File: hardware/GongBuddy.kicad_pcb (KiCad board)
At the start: 2 copper layers, 50 x 80 mm, 51 parts, among them J1 USB_B_Mini, J3 2908-05WB-MG, J4 Conn_01x15, J5 Conn_01x02, J7 Conn_Coaxial, J8 Conn_01x15, Q1 MMBT3904, U1 TPS7A19, U2 USBLC6-2SC6, U3 MCP73831T-2ACI_OT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

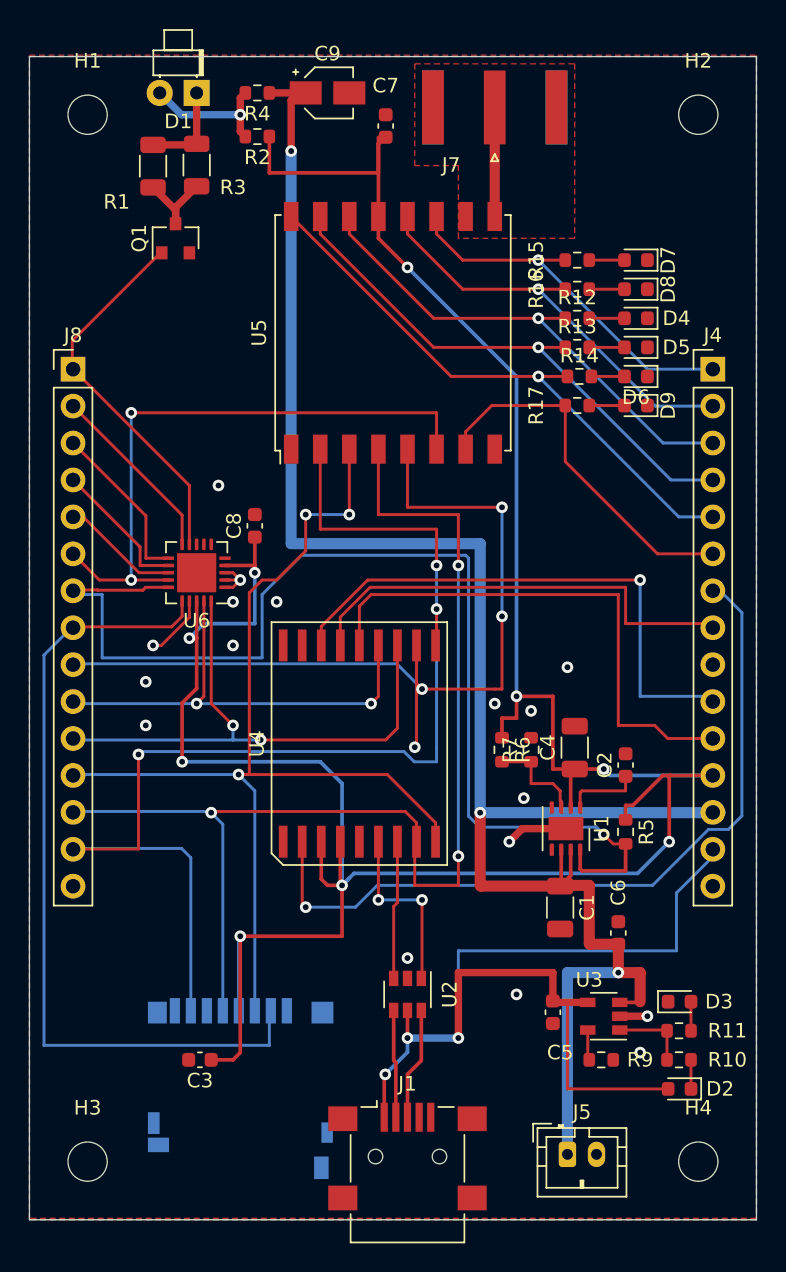
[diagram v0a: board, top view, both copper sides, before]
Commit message: Updated the mechanical design, step files, etc.
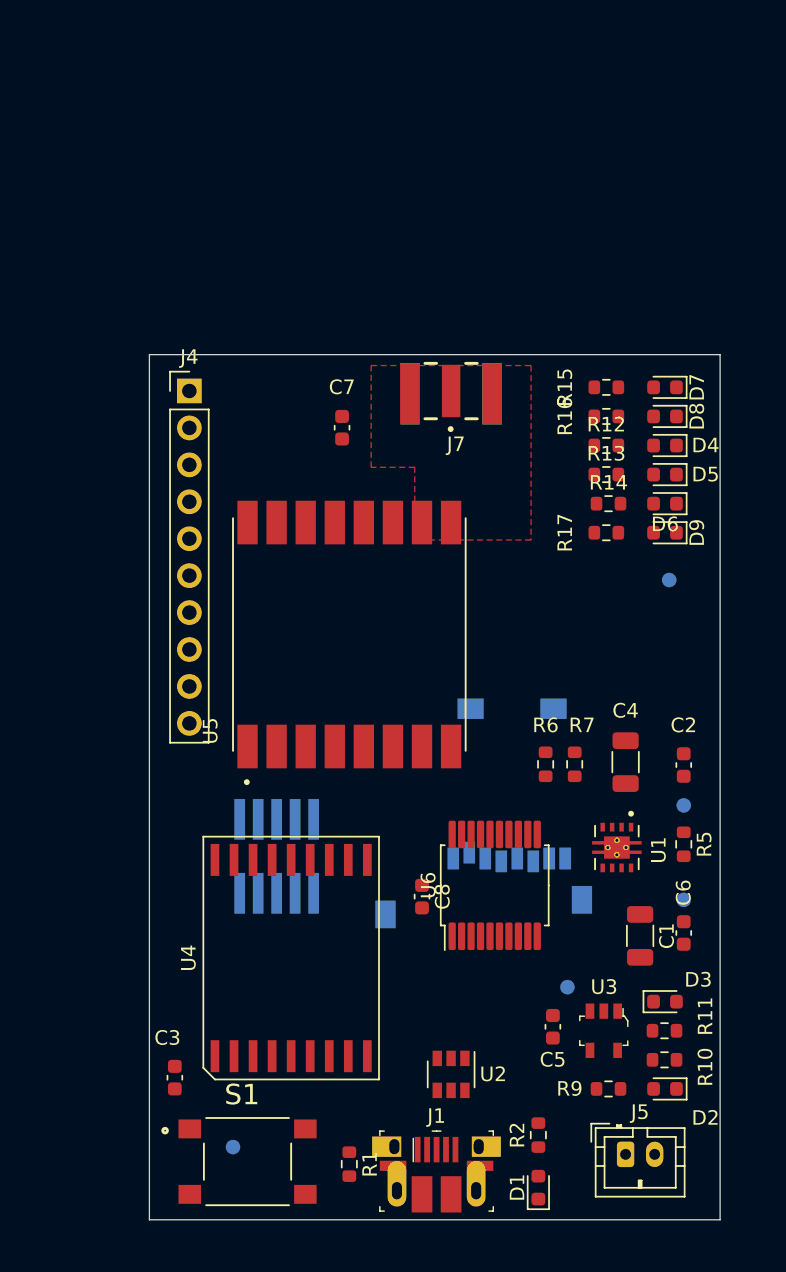
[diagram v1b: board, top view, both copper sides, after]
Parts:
- removed C9: 100u, Capacitor_SMD:CP_Elec_3x5.3
- removed H1, H2, H3, H4: MountingHole, MountingHole:MountingHole_2.7mm_M2.5
- removed J8: Conn_01x15, Connector_PinHeader_2.54mm:PinHeader_1x15_P2.54mm_Vertical
- removed Q1: MMBT3904, Package_TO_SOT_SMD:SOT-23
- removed R3: 50, Resistor_SMD:R_1206_3216Metric
- removed R4: 0, Resistor_SMD:R_0603_1608Metric
- added J2: Conn_ARM_JTAG_SWD_10, KicadFootprint:CortexSWD, B.Cu at (47.0, 115.0)
- added S1: PTS645SK50SMTR92LFS, mechanical:SW_PTS645SK50SMTR92LFS, F.Cu at (45.0, 136.0)
- added TP1: TestPoint, TestPoint:TestPoint_Pad_D1.0mm, B.Cu at (44.0, 135.0)
- added TP2: TestPoint, TestPoint:TestPoint_Pad_D1.0mm, B.Cu at (75.0, 111.5)
- added TP3: TestPoint, TestPoint:TestPoint_Pad_D1.0mm, B.Cu at (67.0, 124.0)
- added TP4: TestPoint, TestPoint:TestPoint_Pad_D1.0mm, B.Cu at (75.0, 118.0)
- added TP5: TestPoint, TestPoint:TestPoint_Pad_D1.0mm, B.Cu at (74.0, 96.0)
- D1: footprint LED_THT:LED_D1.8mm_W1.8mm_H2.4mm_Horizontal_O1.27mm_Z1.6mm -> LED_SMD:LED_0603_1608Metric
- J1: value USB_B_Mini -> 10103594-0001LF; footprint Connector_USB:USB_Mini-B_Lumberg_2486_01_Horizontal -> digikey-footprints:USB_Micro_B_Female_10103594-0001LF
- J3: footprint KicadFootprint:AMPHENOL_1140084168 -> digikey-footprints:MicroSD_2908-05WB-MG
- J4: value Conn_01x15 -> Conn_01x10; footprint Connector_PinHeader_2.54mm:PinHeader_1x15_P2.54mm_Vertical -> Connector_PinHeader_2.54mm:PinHeader_1x10_P2.54mm_Vertical
- J7: footprint Connector_Coaxial:SMA_Amphenol_132289_EdgeMount -> KicadFootprint:SAMTEC_SMA-J-P-H-ST-EM1
- R1: value 50 -> 330; footprint Resistor_SMD:R_1206_3216Metric -> Resistor_SMD:R_0603_1608Metric
- R2: value 0 -> 330
- U1: footprint Package_SON:HVSON-8-1EP_3x3mm_P0.65mm_EP1.6x2.4mm -> KicadFootprint:IC_DRV8601DRBT
- U3: footprint Package_TO_SOT_SMD:SOT-23-5 -> digikey-footprints:SOT-753
- U5: footprint RF_Module:HOPERF_RFM9XW_SMD -> KicadFootprint:XCVR_RFM95W-915S2
- U6: value MCP23008-xML -> MCP23S08; footprint Package_DFN_QFN:QFN-20-1EP_4x4mm_P0.5mm_EP2.7x2.7mm -> Package_SO:SSOP-20_5.3x7.2mm_P0.65mm
- moved D1 78.9 mm to (65.0, 137.8), turned to 90 degrees
- moved R2 71.3 mm to (65.0, 134.2), turned to 90 degrees
- moved R1 70.0 mm to (52.0, 136.2)
- moved J4 36.0 mm to (41.0, 83.0)
- moved U6 29.7 mm to (62.0, 117.0), turned to 90 degrees
- moved C8 28.0 mm to (57.0, 117.8), turned to 270 degrees
- moved C7 21.0 mm to (51.5, 85.5)
- moved U5 21.0 mm to (52.0, 99.8)
- moved J7 19.7 mm to (59.0, 83.0), turned to 180 degrees
- moved J3 18.5 mm to (59.1, 115.2)
- moved U4 15.5 mm to (48.0, 122.0)
- moved D4 8.98 mm to (73.7, 86.8)
- moved D5 8.98 mm to (73.7, 88.8)
- moved D6 8.98 mm to (73.7, 90.8)
- moved D7 8.98 mm to (73.7, 82.8)
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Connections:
- D1 pad 1: Net-(D1-Pad1) -> GND
- J4 pad 1: /DIO3 -> /DIO0
- J4 pad 10: /SWD_IO -> GND
- J4 pad 2: /DIO4 -> /DIO1
- J4 pad 3: /DIO0 -> /IO_INT
- J4 pad 4: /DIO1 -> /IO_CS
- J4 pad 5: /DIO2 -> /LORA_CS
- J4 pad 6: /DIO5 -> /SD_CS
- J4 pad 7: /VDD_OUT -> /SPI_MOSI
- J4 pad 8: /SWD_CLK -> /SPI_CLK
- J4 pad 9: GND -> /SPI_MISO
- R1 pad 1: Net-(D1-Pad1) -> VCC
- R1 pad 2: Net-(Q1-Pad3) -> /BUTTON1
- R2 pad 1: VCC -> /LED1
- U4 pad 10: /SPI_MISO -> /SPI_MOSI
- U4 pad 11: /LORA_CS -> /IO_CS
- U4 pad 12: /I2C_SDA -> /IO_RESET
- U4 pad 13: /I2C_SCL -> /IO_INT
- U4 pad 9: /SPI_MOSI -> /SPI_MISO
- U6 pad 1: GND -> /SPI_CLK
- U6 pad 10: Net-(J8-Pad2) -> (no net)
- U6 pad 11: Net-(J8-Pad3) -> (no net)
- U6 pad 12: Net-(J8-Pad4) -> /DIO0
- U6 pad 13: Net-(J8-Pad5) -> /DIO1
- U6 pad 14: /LORA_RESET -> /LED1
- U6 pad 15: /PG -> /BUTTON1
- U6 pad 16: /SD_CS -> /LORA_CS
- U6 pad 17: GND -> /LORA_RESET
- U6 pad 18: VCC -> /PG
- U6 pad 19: /I2C_SCL -> /SD_CS
- U6 pad 2: GND -> /SPI_MOSI
- U6 pad 20: /I2C_SDA -> VCC
- U6 pad 3: GND -> /SPI_MISO
- U6 pad 4: VCC -> GND
- U6 pad 5: Net-(U6-Pad5) -> GND
- U6 pad 6: Net-(U6-Pad6) -> /IO_RESET
- U6 pad 7: Net-(U6-Pad7) -> /IO_CS
- U6 pad 8: Net-(U6-Pad8) -> /IO_INT
- U6 pad 9: /BIG_LED -> GND
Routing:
- net VCC: track 194.9 -> 0.00 mm, vias 9 -> 0
- net /VBAT: track 129.7 -> 0.00 mm, vias 3 -> 0
- net /SPI_MISO: track 83.0 -> 0.00 mm, vias 3 -> 0
- net /SPI_CLK: track 80.9 -> 0.00 mm, vias 3 -> 0
- net /PG: track 79.7 -> 0.00 mm, vias 1 -> 0
- net /SPI_MOSI: track 71.9 -> 0.00 mm, vias 3 -> 0
- net VBUS: track 69.0 -> 0.00 mm, vias 3 -> 0
- net /LORA_CS: track 63.5 -> 0.00 mm, vias 4 -> 0
- net /SD_CS: track 56.4 -> 0.00 mm
- net /VDD_OUT: track 53.3 -> 0.00 mm, vias 1 -> 0
- net /LORA_RESET: track 42.4 -> 0.00 mm, vias 2 -> 0
- net /DIO2: track 40.1 -> 0.00 mm, vias 1 -> 0
- net /I2C_SDA: track 38.7 -> 0.00 mm, vias 2 -> 0
- net /SWD_IO: track 38.2 -> 0.00 mm, vias 1 -> 0
- net /DIO1: track 37.6 -> 0.00 mm, vias 1 -> 0
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- removed copper zone on B.Cu, net GND
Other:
- board size 50 x 80 mm -> 39.2 x 59.5 mm

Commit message: Added more files.
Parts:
- added TP10: TestPoint, TestPoint:TestPoint_Pad_D1.0mm, B.Cu at (66.0, 84.0)
- added TP11: TestPoint, TestPoint:TestPoint_Pad_D1.0mm, B.Cu at (67.0, 134.5)
- added TP12: TestPoint, TestPoint:TestPoint_Pad_D1.0mm, B.Cu at (66.0, 91.8)
- added TP6: TestPoint, TestPoint:TestPoint_Pad_D1.0mm, B.Cu at (42.5, 125.5)
- added TP7: TestPoint, TestPoint:TestPoint_Pad_D1.0mm, B.Cu at (52.0, 132.5)
- added TP8: TestPoint, TestPoint:TestPoint_Pad_D1.0mm, B.Cu at (66.0, 89.7)
- added TP9: TestPoint, TestPoint:TestPoint_Pad_D1.0mm, B.Cu at (66.0, 81.8)
- moved C3 23.6 mm to (56.6, 113.4)
- moved TP1 9.45 mm to (45.0, 125.6)
- moved TP4 2.06 mm to (73.0, 117.5)
- moved TP5 1.84 mm to (73.3, 94.3)
- moved R14 1.66 mm to (68.5, 89.8)
- moved C2 1.58 mm to (73.5, 108.2)
- moved C6 1.58 mm to (73.5, 120.8), turned to 270 degrees
- moved D4 1.57 mm to (72.5, 85.8)
- moved D5 1.57 mm to (72.5, 87.8)
- moved D6 1.57 mm to (72.5, 89.8)
- moved D7 1.57 mm to (72.5, 81.8)
- moved D8 1.57 mm to (72.5, 83.8)
- moved D9 1.57 mm to (72.5, 91.8)
- moved C7 1.56 mm to (52.4, 86.8)
- moved R12 1.54 mm to (68.5, 85.8)
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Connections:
- J4 pad 7: /SPI_MOSI -> /SPI_CLK
- J4 pad 8: /SPI_CLK -> /SPI_MOSI
- U1 pad 10: (no net) -> GND
- U1 pad 11: (no net) -> GND
- U1 pad 12: (no net) -> GND
- U1 pad 13: (no net) -> GND
- U6 pad 12: /DIO0 -> /PG
- U6 pad 13: /DIO1 -> /DIO0
- U6 pad 14: /LED1 -> /DIO1
- U6 pad 15: /BUTTON1 -> /LED1
- U6 pad 16: /LORA_CS -> /BUTTON1
- U6 pad 17: /LORA_RESET -> /SD_CS
- U6 pad 18: /PG -> /LORA_RESET
- U6 pad 19: /SD_CS -> /LORA_CS
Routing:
- net /DIO0: track 0.00 -> 71.8 mm, vias 0 -> 3
- net /DIO1: track 0.00 -> 68.0 mm, vias 0 -> 4
- net GND: track 0.00 -> 67.1 mm, vias 0 -> 61
- net /SPI_CLK: track 0.00 -> 63.1 mm, vias 0 -> 4
- net /IO_INT: track 0.00 -> 61.3 mm, vias 0 -> 3
- net /IO_CS: track 0.00 -> 58.5 mm, vias 0 -> 4
- net /SPI_MISO: track 0.00 -> 58.5 mm, vias 0 -> 4
- net /BUTTON1: track 0.00 -> 49.2 mm, vias 0 -> 3
- net /SD_CS: track 0.00 -> 40.5 mm, vias 0 -> 2
- net /SPI_MOSI: track 0.00 -> 37.2 mm, vias 0 -> 1
- net VBUS: track 0.00 -> 36.2 mm, vias 0 -> 4
- net /LORA_CS: track 0.00 -> 35.3 mm
- net /DIO2: track 0.00 -> 34.8 mm, vias 0 -> 2
- net /VBAT: track 0.00 -> 34.3 mm, vias 0 -> 2
- net /DIO4: track 0.00 -> 30.0 mm, vias 0 -> 2
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- added copper zone on In2.Cu, net GND
- added copper zone on In1.Cu, net VCC
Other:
- board size 39.2 x 59.5 mm -> 39 x 59 mm
- copper layers 2 -> 4
- net class Default: clearance 0.2 -> 0.127; trace_width 0.25 -> 0.1524; via_dia 0.8 -> 0.381; via_drill 0.4 -> 0.2032
- rule trace_clearance: 0.2 -> 0.127
- rule trace_min: 0.2 -> 0.1016
- rule via_min_drill: 0.3 -> 0.2032
- rule via_min_size: 0.4 -> 0.381
- board text added: "GongBuddy Rev B Copyright 2021 Nick Butts"
- board text removed: "GongBuddy Rev A Copyright 2020 Nick Butts"

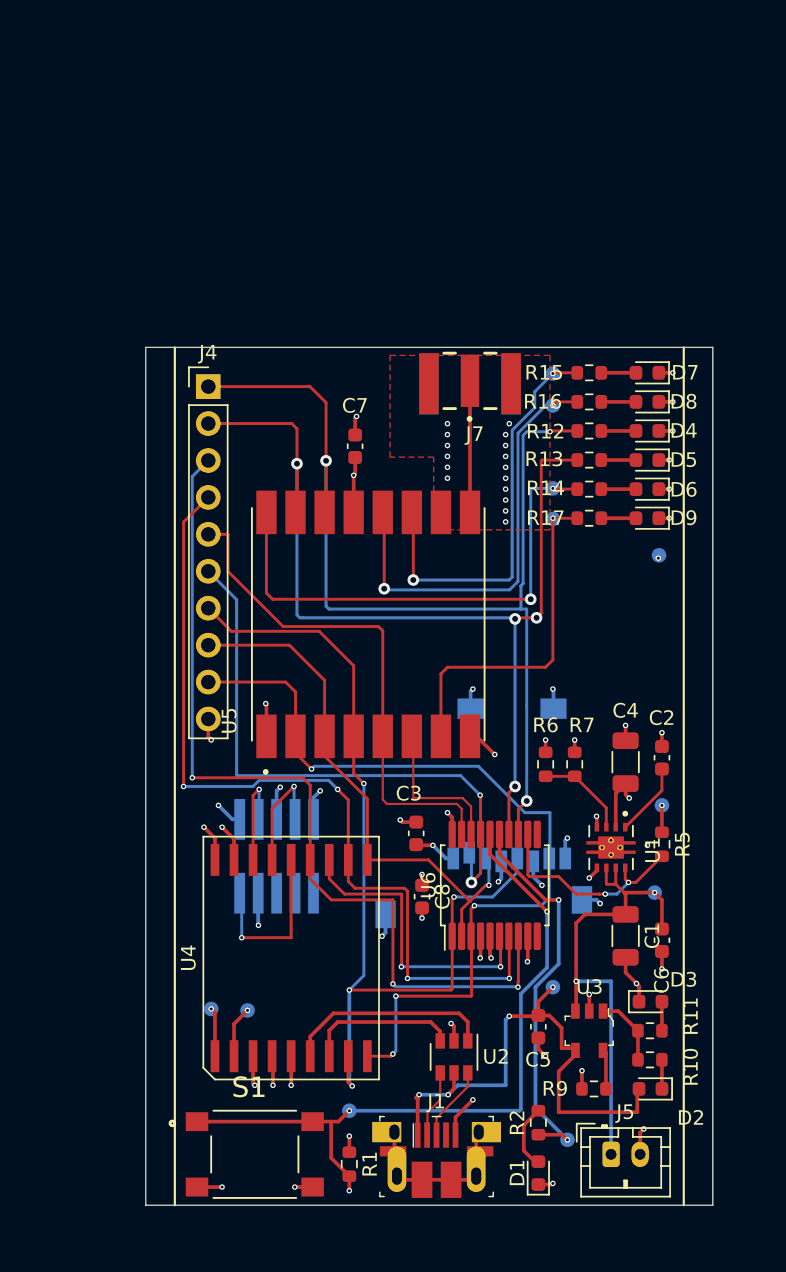
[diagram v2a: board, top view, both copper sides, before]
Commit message: Tweaked layout based on integration with the enclosure.
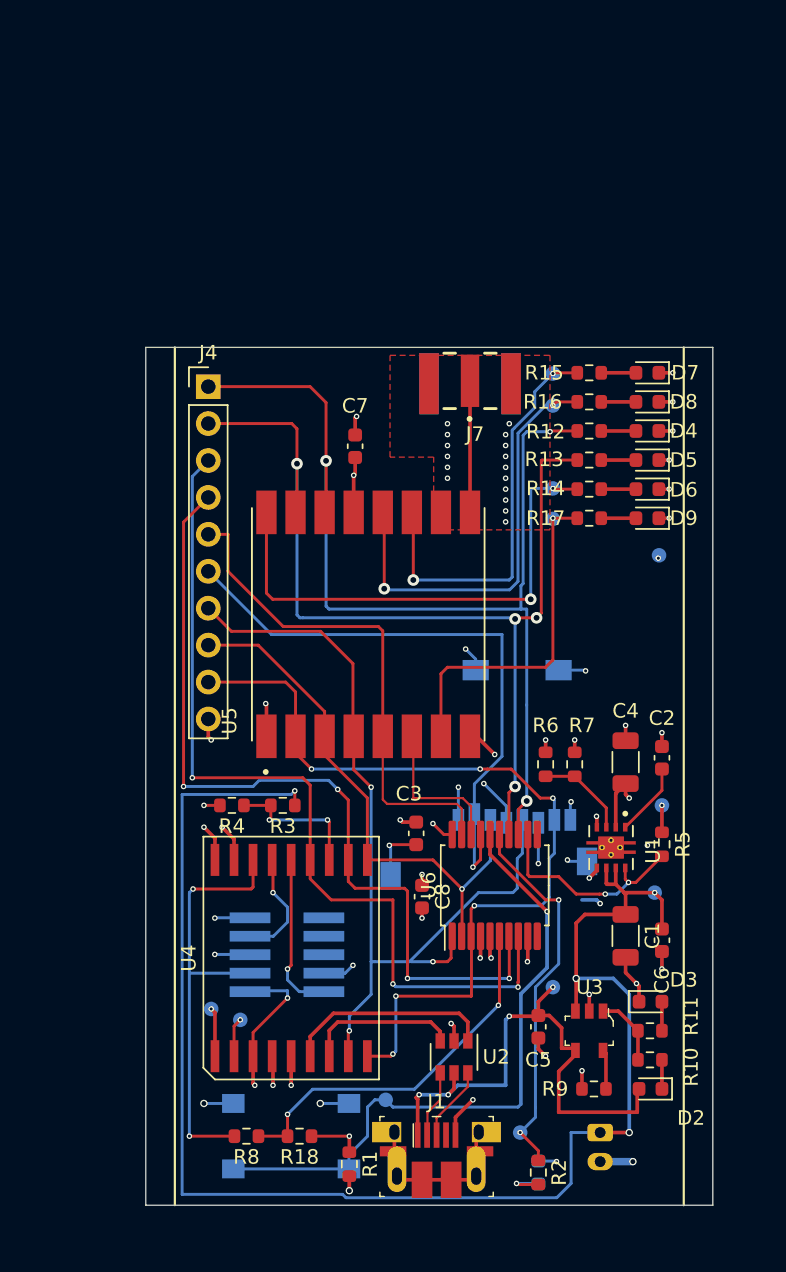
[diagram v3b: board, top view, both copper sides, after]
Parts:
- added R18: 10k, Resistor_SMD:R_0603_1608Metric, F.Cu at (48.6, 134.2)
- added R3: 49.9, Resistor_SMD:R_0603_1608Metric, F.Cu at (47.4, 111.5)
- added R4: 24.3, Resistor_SMD:R_0603_1608Metric, F.Cu at (43.9, 111.5)
- added R8: DNP, Resistor_SMD:R_0603_1608Metric, F.Cu at (44.9, 134.2)
- D1, J5, S1: moved to B.Cu
- moved J2 6.81 mm to (47.7, 121.8), turned to 90 degrees
- moved R2 3.43 mm to (65.0, 136.8), turned to 270 degrees
- moved TP11 3.29 mm to (63.8, 134.0)
- moved S1 2.80 mm to (48.0, 134.2)
- moved J3 2.67 mm to (59.5, 112.5)
- moved TP7 2.61 mm to (54.5, 131.8)
- moved J5 1.68 mm to (69.2, 134.0), turned to 270 degrees
- moved TP1 0.82 mm to (44.5, 126.2)
- turned D1 to 270 degrees
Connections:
- U4 pad 12: /IO_RESET -> /VBAT_ADC
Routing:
- net /VBAT: track 34.3 -> 104.5 mm, vias 2 -> 4
- net /SWD_IO: track 7.11 -> 30.4 mm, vias 1 -> 2
- net VCC: track 23.0 -> 33.7 mm
- net /VBAT_ADC: track 0.00 -> 9.69 mm, vias 0 -> 2
- net GND: track 67.1 -> 75.0 mm, vias 61 -> 63
- net /IO_RESET: track 20.7 -> 25.9 mm
- net /SPI_CLK: track 63.1 -> 61.1 mm, vias 4 -> 3
- net /BUTTON1: track 49.2 -> 47.2 mm
- net /VDD_OUT: track 3.54 -> 2.68 mm
- net Net-(D1-Pad2): track 4.47 -> 3.65 mm, vias 0 -> 1
- net /SPI_MISO: track 58.5 -> 59.3 mm, vias 4 -> 6
- net /SD_CS: track 40.5 -> 41.3 mm, vias 2 -> 1
- net /NRST: track 11.9 -> 11.2 mm
- net /LED1: track 26.9 -> 26.3 mm

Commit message: Added ESD diodes and cleaned up the silkscreen.
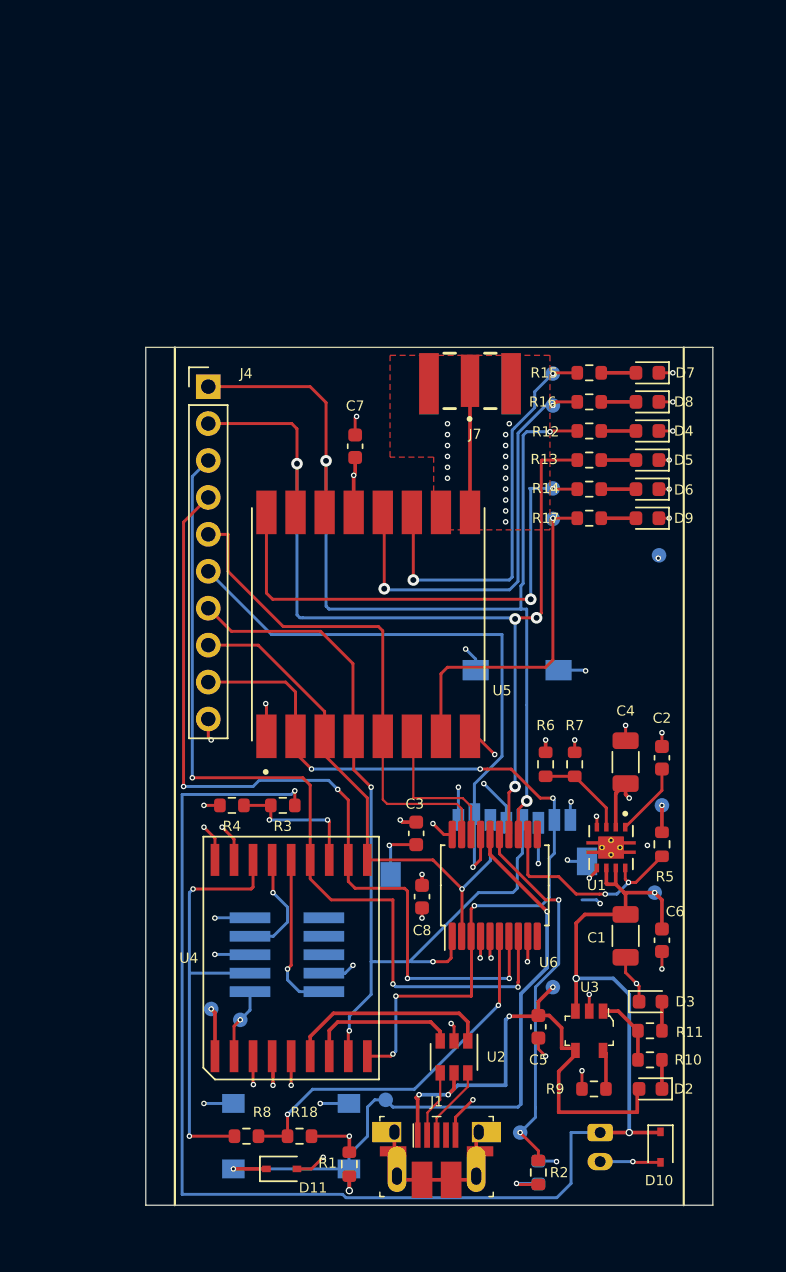
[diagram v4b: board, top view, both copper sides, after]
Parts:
- added D10: DESD5V0U1BA-7, Diode_SMD:D_SOD-323, F.Cu at (73.4, 135.0)
- added D11: DESD5V0U1BA-7, Diode_SMD:D_SOD-323, F.Cu at (47.4, 136.5)
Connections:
- J1 pad 4: Net-(J1-Pad4) -> (no net)
- J2 pad 1: VCC -> /VDD_OUT
- J2 pad 6: Net-(J2-Pad6) -> (no net)
- J2 pad 7: Net-(J2-Pad7) -> (no net)
- J2 pad 8: Net-(J2-Pad8) -> (no net)
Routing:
- net VCC: track 33.7 -> 25.6 mm, vias 12 -> 11
- net GND: track 75.0 -> 79.1 mm, vias 63 -> 64
- net /BUTTON1: track 47.2 -> 49.5 mm, vias 3 -> 4
- net /VDD_OUT: track 2.68 -> 4.90 mm
- net /VBAT: track 104.5 -> 106.6 mm
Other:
- board text added: "DIO0"
- board text added: "DIO1"
- board text added: "GND"
- board text added: "IO_CS"
- board text added: "IO_INT"
- board text added: "LORA_CS"
- board text added: "SD_CS"
- board text added: "SPI_CLK"
- board text added: "SPI_MISO"
- board text added: "SPI_MOSI"
